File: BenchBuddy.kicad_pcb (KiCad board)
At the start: 2 copper layers, 69.1 x 53.3 mm, 0 parts

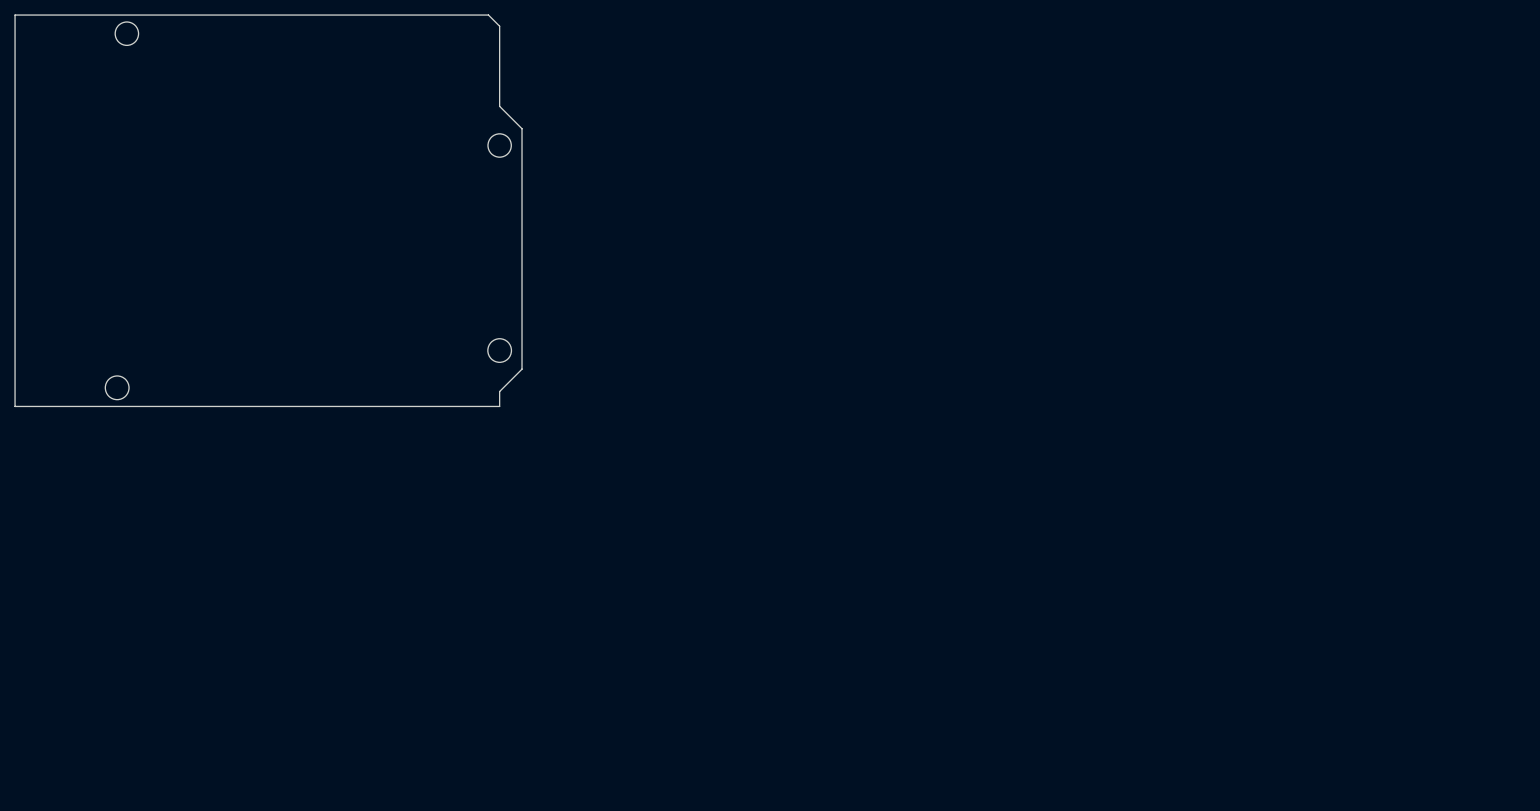
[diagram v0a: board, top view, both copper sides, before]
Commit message: Preliminary Module Layouts
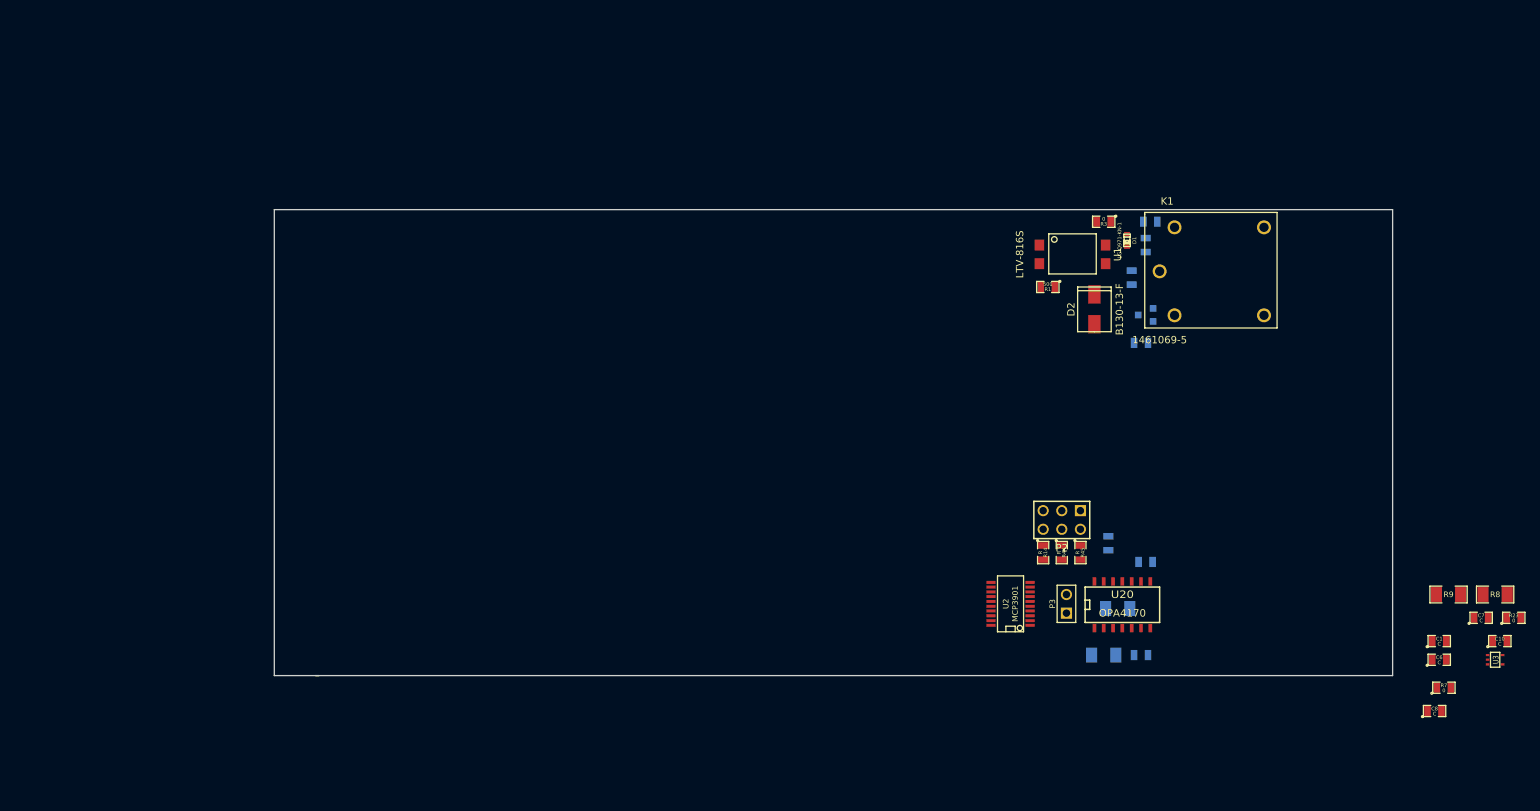
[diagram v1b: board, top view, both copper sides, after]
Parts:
- added C1: C, SM0805, F.Cu at (297.8, 164.5)
- added C10: C, SM0805, F.Cu at (306.1, 164.5)
- added C6: C, SM0805, F.Cu at (297.8, 167.0)
- added C7: C, SM0805, F.Cu at (303.5, 161.3)
- added C8: C, SM0805, F.Cu at (297.2, 174.0)
- added C9: C, SM0805, B.Cu at (252.7, 151.1)
- added D1: LG Q971-KN-1, LED-0603, F.Cu at (255.3, 109.9)
- added D2: B130-13-F, SMA, F.Cu at (250.8, 121.3)
- added K1: 1461069-5, TE-SPDT, F.Cu at (259.7, 111.1)
- added P2: CONN_3X2, pin_array_3x2, F.Cu at (246.4, 148.0)
- added P3: CONN_2, PIN_ARRAY_2X1, F.Cu at (247.0, 159.4)
- added Q1: 2N3904, SOT23EBC, B.Cu at (257.8, 120.0)
- added R1: 500, SM0805, F.Cu at (244.5, 116.2)
- added R10: R, SM1206, B.Cu at (254.0, 160.0)
- added R11: R, SM1206, B.Cu at (252.1, 166.4)
- added R12: R, SM0805, B.Cu at (257.2, 166.4)
- added R13: R, SM0805, B.Cu at (257.8, 153.7)
- added R14: R, SM0805, F.Cu at (243.8, 152.4)
- added R2: 200, SM0805, B.Cu at (255.9, 114.9)
- added R23: 0, SM0805, F.Cu at (308.0, 161.3)
- added R3: 0, SM0805, F.Cu at (252.1, 107.3)
- added R4: 100, SM0805, B.Cu at (257.8, 110.5)
- added R44: R, SM0805, F.Cu at (246.4, 152.4)
- added R45: R, SM0805, F.Cu at (248.9, 152.4)
- added R5: 0, SM0805, B.Cu at (258.4, 107.3)
- added R6: 0, SM0805, B.Cu at (257.2, 123.8)
- added R7: 0, SM0805, F.Cu at (298.4, 170.8)
- added R8: R, SM1206, F.Cu at (305.4, 158.1)
- added R9: R, SM1206, F.Cu at (299.1, 158.1)
- added U1: LTV-816S, 4-SMD, F.Cu at (245.7, 111.8)
- added U2: MCP3901, SSOP20, F.Cu at (239.4, 159.4)
- added U20: OPA4170, SO14N, F.Cu at (254.6, 159.4)
- added U3: LMT84, SOT353, F.Cu at (305.4, 167.0)
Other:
- board size 69.1 x 53.3 mm -> 152.4 x 63.5 mm
- copper layers 2 -> 4
- rule pad_to_mask_clearance: 0 -> 0.254
- rule trace_min: 0.254 -> 0.1524
- rule via_min_drill: 0.508 -> 0.3302
- rule via_min_size: 0.889 -> 0.508

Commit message: Plug Placement
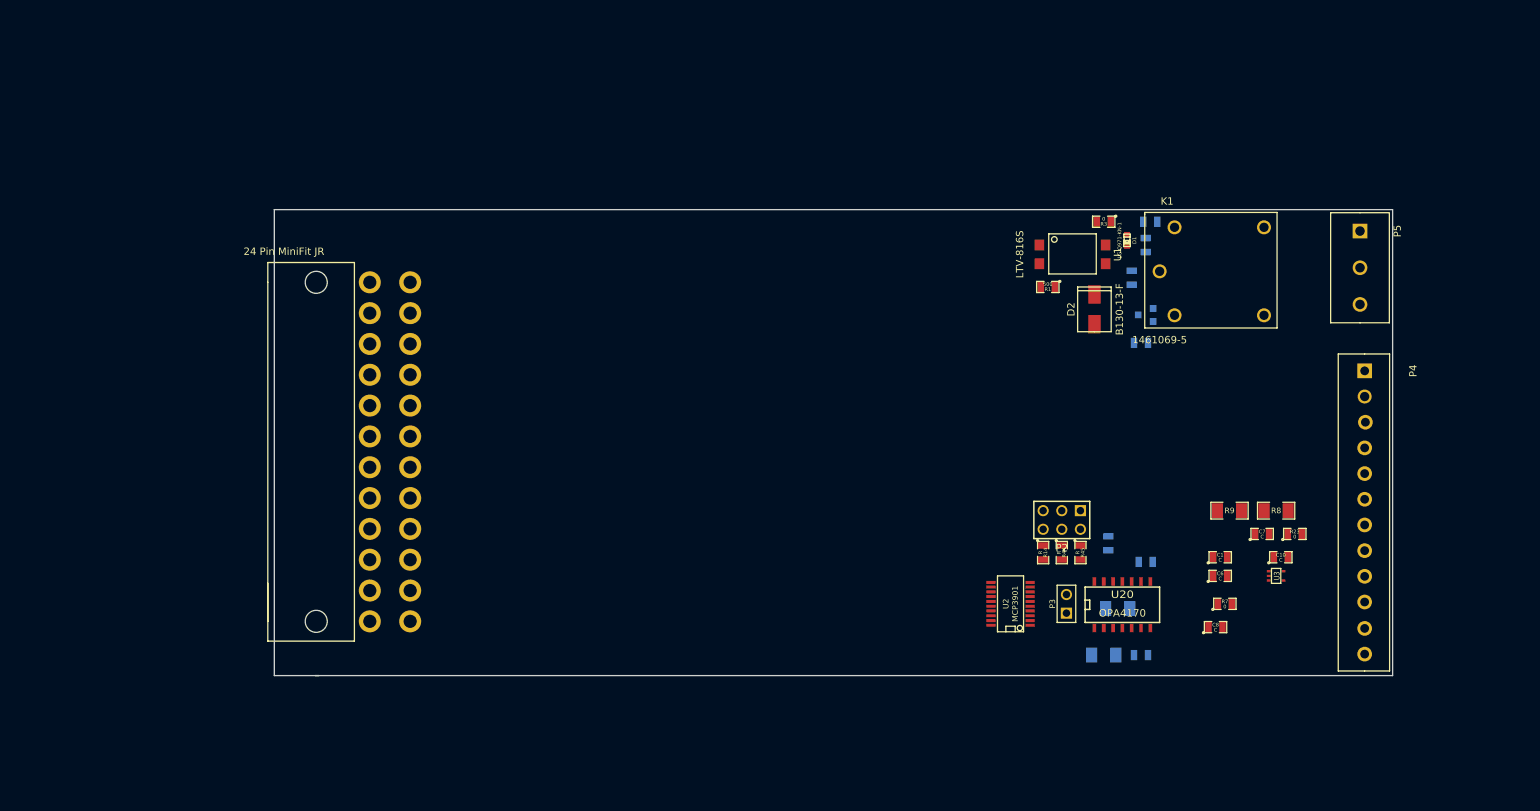
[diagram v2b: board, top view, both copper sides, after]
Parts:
- added P1: 24 Pin MiniFit JR, ATX_Header, F.Cu at (144.8, 115.6)
- added P4: 12 Pin Terminal Block, 12pinTB, F.Cu at (287.7, 127.6)
- added P5: 3 Pin TB, 3pinTB, F.Cu at (287.0, 108.6)
- moved C8 32.0 mm to (267.3, 162.6)
- moved R8 32.0 mm to (275.6, 146.7)
- moved U3 32.0 mm to (275.6, 155.6)
- moved R23 32.0 mm to (278.1, 149.9)
- moved C1 32.0 mm to (268.0, 153.0)
- moved C10 32.0 mm to (276.2, 153.0)
- moved C6 32.0 mm to (268.0, 155.6)
- moved R7 32.0 mm to (268.6, 159.4)
- moved R9 32.0 mm to (269.2, 146.7)
- moved C7 32.0 mm to (273.7, 149.9)
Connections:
- K1 pad 1: (no net) -> /Relay/RELAY_COM
- K1 pad 3: (no net) -> /Relay/RELAY_NO
- K1 pad 4: (no net) -> /Relay/RELAY_NC
- U20 pad 10: (no net) -> /Thermocouple/TC IN -
- U20 pad 5: (no net) -> /Thermocouple/TC IN +

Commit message: Power Modification Module
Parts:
- added C11: C, SM1206, F.Cu at (192.9, 134.1)
- added C12: C, SM0805, F.Cu at (280.4, 163.2)
- added C13: C, SM0805, F.Cu at (258.4, 155.7)
- added C2: C, SM1206, F.Cu at (204.9, 134.1)
- added C3: C, SM1206, F.Cu at (198.9, 134.1)
- added C4: C, SM0805, F.Cu at (196.1, 139.1)
- added C5: C, SM0805, F.Cu at (192.3, 139.1)
- added D5: B130-13-F, SMA, F.Cu at (263.8, 165.5)
- added L1: INDUCTOR, SM1210L, F.Cu at (195.2, 129.8)
- added L2: INDUCTOR, SM1210L, F.Cu at (202.2, 129.8)
- added L3: INDUCTOR, SM1210L, F.Cu at (186.4, 134.5)
- added L4: INDUCTOR, SM1210L, F.Cu at (171.2, 135.5)
- added Q2: DMN65D8L-7, SOT23GDS, F.Cu at (242.6, 161.7)
- added Q3: AOD476, DPAK2, F.Cu at (273.7, 159.9)
- added Q4: AOD476, DPAK2, F.Cu at (266.3, 159.9)
- added R15: R, SM0805, F.Cu at (188.6, 139.1)
- added R16: R, SM0805, F.Cu at (203.5, 137.0)
- added R17: R, SM0805, F.Cu at (237.5, 165.2)
- added R18: R, SM1206, F.Cu at (273.1, 165.5)
- added R19: R, SM0805, F.Cu at (196.1, 137.0)
- added R22: R, SM0805, F.Cu at (199.8, 137.0)
- added R24: R, SM0805_blob, F.Cu at (184.8, 137.2)
- added R25: R, SM0805, F.Cu at (188.6, 137.0)
- added R26: R, SM0805, F.Cu at (207.3, 137.0)
- added R27: R, SM0805, F.Cu at (184.8, 139.1)
- added R28: R, SM0805, F.Cu at (192.3, 137.0)
- added R29: R, SM0805_blob, F.Cu at (187.3, 158.4)
- added R30: R, SM0805_blob, F.Cu at (192.4, 158.4)
- added R31: R, SM0805_blob, F.Cu at (194.9, 158.4)
- added R32: R, SM0805_blob, F.Cu at (197.5, 158.4)
- added R33: R, SM0805_blob, F.Cu at (200.0, 158.4)
- added R34: R, SM0805_blob, F.Cu at (170.6, 117.7)
- added R35: R, SM0805_blob, F.Cu at (173.1, 117.7)
- added R36: R, SM0805_blob, F.Cu at (175.5, 117.7)
- added R37: R, SM0805_blob, F.Cu at (178.2, 117.7)
- added R38: R, SM0805_blob, F.Cu at (180.7, 117.7)
- added R39: R, SM0805_blob, F.Cu at (183.3, 117.7)
- added R40: R, SM0805_blob, F.Cu at (187.3, 117.7)
- added R41: R, SM0805_blob, F.Cu at (202.6, 117.7)
- added R42: R, SM0805_blob, F.Cu at (205.1, 117.7)
- added R43: R, SM0805_blob, F.Cu at (184.8, 154.3)
- added R46: R, SM0805_blob, F.Cu at (192.4, 117.7)
- added R47: R, SM0805_blob, F.Cu at (194.9, 117.7)
- added R48: R, SM0805_blob, F.Cu at (179.7, 158.4)
- added R49: R, SM0805_blob, F.Cu at (182.2, 158.4)
- added R50: R, SM0805_blob, F.Cu at (184.8, 158.4)
- added R51: R, SM0805_blob, F.Cu at (200.0, 117.7)
- added SW1: SWITCH_INV, BB_switch, F.Cu at (164.0, 167.0)
- added TH1: THERMISTOR, SM1812, B.Cu at (144.7, 157.5)
- added TH2: THERMISTOR, SM1812, B.Cu at (145.4, 140.8)
- added TH3: THERMISTOR, SM1812, B.Cu at (145.4, 124.0)
- added TH4: THERMISTOR, SM1812, B.Cu at (164.0, 157.5)
- added TH5: MINISMDC050F-2, SM1812, F.Cu at (257.6, 165.2)
- added U12: ARDUINOPINS, Arduino, F.Cu at (173.4, 141.0)
- added U4: MCP4801, SO8N, F.Cu at (236.0, 155.4)
- moved P4 38.9 mm to (287.3, 166.5), turned to 90 degrees
- moved P3 20.3 mm to (229.9, 148.5)
- moved C7 18.1 mm to (272.2, 131.8)
- moved R23 18.1 mm to (276.6, 131.8)
- moved C1 18.1 mm to (266.4, 135.0)
- moved C10 18.1 mm to (274.7, 135.0)
- moved C6 18.1 mm to (266.4, 137.5)
- moved C8 18.1 mm to (265.8, 144.5)
- moved R7 18.1 mm to (267.1, 141.4)
- moved R8 18.1 mm to (274.1, 128.7)
- moved R9 18.1 mm to (267.7, 128.7)
- moved U3 18.1 mm to (274.1, 137.5)
- moved P2 13.1 mm to (239.1, 137.0)
- moved R10 13.1 mm to (246.8, 149.1)
- moved R11 13.1 mm to (244.9, 155.4)
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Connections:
- U2 pad 17: /Arduino/ADC_CS_N -> /Arduino/~ADC_CS

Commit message: November 25 Update
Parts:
- added C14: C, SM0805, F.Cu at (174.8, 137.3)
- added C15: C, SM0805, F.Cu at (178.6, 137.3)
- added C16: C, SM0805, F.Cu at (171.1, 137.3)
- added C17: C, SM0805, F.Cu at (182.2, 137.3)
- added C18: C, SM0805, F.Cu at (200.9, 137.3)
- added C19: C, SM0805, F.Cu at (204.6, 137.3)
- added C20: C, SM0805, F.Cu at (208.4, 137.3)
- added C21: C, SM0805, F.Cu at (193.4, 137.3)
- added C22: C, SM0805, F.Cu at (219.1, 110.0)
- added C23: C, SM0805, F.Cu at (189.7, 137.3)
- added C24: C, SM0805, F.Cu at (185.9, 137.3)
- added C25: C, SM0805, F.Cu at (197.2, 137.3)
- added U11: LM317, TO220, F.Cu at (200.5, 149.7)
- added U6: LM317, TO220, F.Cu at (168.4, 149.4)
- added U7: LM337T, TO220, F.Cu at (168.1, 126.7)
- added U8: LM337T, TO220, F.Cu at (200.5, 126.6)
- L1, L2, L4: value INDUCTOR -> CM322522-220KL
- SW1: value SWITCH_INV -> OS102011MA1QN1
- TH1, TH2, TH3, TH4: value THERMISTOR -> MINISMDC050F-2
- moved L2 44.3 mm to (215.5, 87.5)
- moved C2 44.3 mm to (218.2, 91.8)
- moved C3 44.3 mm to (212.2, 91.8)
- moved C4 44.3 mm to (209.4, 96.8)
- moved C5 44.3 mm to (205.6, 96.8)
- moved R15 44.3 mm to (201.9, 96.8)
- moved R24 44.3 mm to (198.1, 94.9)
- moved R27 44.3 mm to (198.1, 96.8)
- moved C11 44.3 mm to (206.2, 91.8)
- moved L1 44.3 mm to (208.5, 87.5)
- moved L3 44.3 mm to (199.8, 92.2)
- moved L4 44.3 mm to (184.5, 93.2)
- moved R19 44.3 mm to (209.4, 94.7)
- moved R22 44.3 mm to (213.1, 94.7)
- moved R25 44.3 mm to (201.9, 94.7)
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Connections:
- R19 pad 1: AGND -> FE_V-
- R22 pad 1: AGND -> N-00000132
- R22 pad 2: N-00000129 -> /PowerAdjustmentMonitor/V+_ADJ

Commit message: Power Modification Module (check diodes)
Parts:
- added D10: MMBD914-7-F, SOT23-DIODE, F.Cu at (179.7, 130.6)
- added D11: MMBD914-7-F, SOT23-DIODE, B.Cu at (225.4, 166.9)
- added D12: MMBD914-7-F, SOT23-DIODE, B.Cu at (221.4, 109.3)
- added D3: MMBD914-7-F, SOT23-DIODE, F.Cu at (183.4, 141.6)
- added D4: DIODESCH, SMA, B.Cu at (143.4, 131.3)
- added D6: MMBD914-7-F, SOT23-DIODE, B.Cu at (225.6, 109.3)
- added D7: MMBD914-7-F, SOT23-DIODE, F.Cu at (183.0, 133.2)
- added D8: MMBD914-7-F, SOT23-DIODE, B.Cu at (230.0, 166.8)
- added D9: MMBD914-7-F, SOT23-DIODE, F.Cu at (179.2, 143.6)
- added R20: R, SM0805, F.Cu at (213.0, 134.6)
- added R21: 5K, EVUE3K, F.Cu at (240.2, 162.8)
- added R52: R, SM0805, F.Cu at (224.3, 134.7)
- added R53: R, SM0805, F.Cu at (179.8, 127.3)
- added R54: 5K, EVUE3K, F.Cu at (235.3, 112.0)
- added R55: 715, SM0805, F.Cu at (231.9, 149.9)
- C11, C3, C4, L3, L4, R16, R17, R28: moved to B.Cu
- R22: value R -> 715; moved to B.Cu
- TH4: moved to F.Cu
- moved R16 88.0 mm to (283.7, 151.9), turned to 270 degrees
- moved C2 86.8 mm to (168.3, 162.8), turned to 180 degrees
- moved L2 82.7 mm to (170.7, 157.0), turned to 90 degrees
- moved L1 77.1 mm to (175.1, 157.0), turned to 270 degrees
- moved R15 77.1 mm to (163.1, 163.3)
- moved L3 69.8 mm to (145.4, 136.0), turned to 180 degrees
- moved C11 67.9 mm to (180.5, 154.7)
- moved L4 65.2 mm to (145.8, 145.7), turned to 180 degrees
- moved C4 62.4 mm to (178.9, 151.3)
- moved R22 52.4 mm to (221.7, 146.4), turned to 270 degrees
- moved R25 49.8 mm to (217.4, 142.1), turned to 270 degrees
- moved R19 42.8 mm to (212.9, 137.4), turned to 180 degrees
- moved R26 38.2 mm to (213.0, 132.2), turned to 180 degrees
- moved R28 34.1 mm to (221.7, 124.8), turned to 90 degrees
- moved C22 33.4 mm to (213.1, 142.9), turned to 180 degrees
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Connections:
- C23 pad 1: (no net) -> AGND
- C23 pad 2: (no net) -> FE_V-
